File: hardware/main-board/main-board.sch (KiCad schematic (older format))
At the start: 12 parts

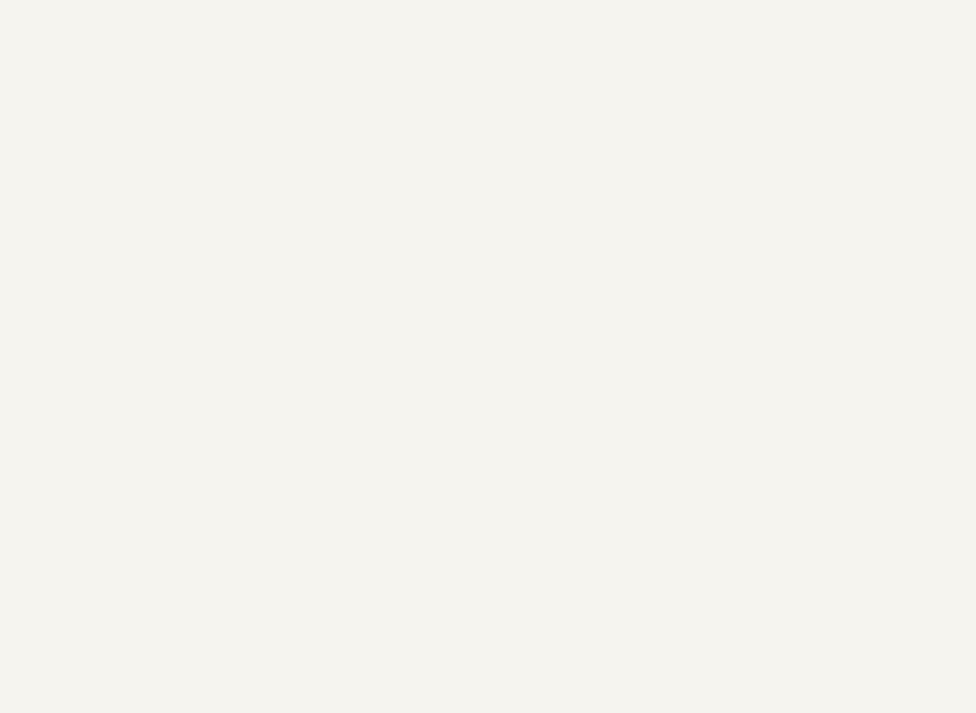
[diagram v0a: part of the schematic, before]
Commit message: Sound to light board completed, PSU board completed
Rev As as ordered
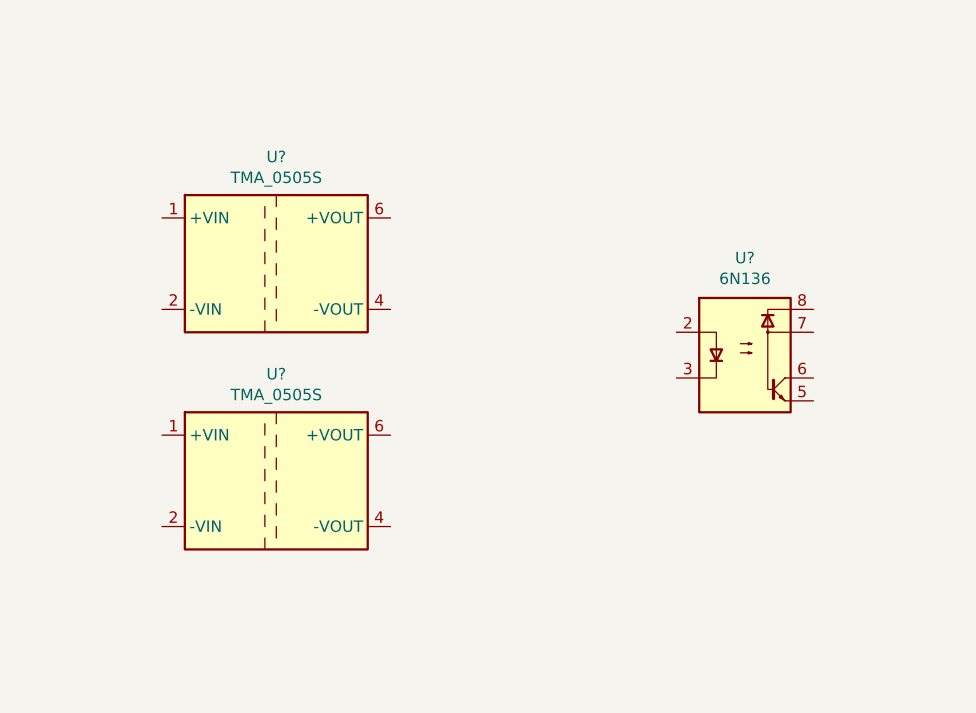
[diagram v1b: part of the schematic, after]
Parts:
- added U? (x2): TMA_0505S, Converter_DCDC:Traco_TMA_DCDCsingle, symbol Regulator_Switching:TMA_0505S
- added U?: 6N136, Package_DIP:DIP-8_W7.62mm, symbol Isolator:6N136
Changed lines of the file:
@@
 NoConn ~ 2600 6800
 NoConn ~ 2600 6900
+$Comp
+L Regulator_Switching:TMA_0505S U?
+U 1 1 5E9BA76B
+P 4000 1650
+F 0 "U?" H 4000 2117 50  0000 C CNN
+F 1 "TMA_0505S" H 4000 2026 50  0000 C CNN
+F 2 "Converter_DCDC:Traco_TMA_DCDCsingle" H 4000 1300 50  0001 C CNN
+F 3 "http://assets.tracopower.com/TMR1/documents/tmr1-datasheet.pdf" H 4000 1150 50  0001 C CNN
+	1    4000 1650
+	1    0    0    -1
+$EndComp
+$Comp
+L Regulator_Switching:TMA_0505S U?
+U 1 1 5E9BC0CB
+P 4000 2600
+F 0 "U?" H 4000 3067 50  0000 C CNN
+F 1 "TMA_0505S" H 4000 2976 50  0000 C CNN
+F 2 "Converter_DCDC:Traco_TMA_DCDCsingle" H 4000 2250 50  0001 C CNN
+F 3 "http://assets.tracopower.com/TMR1/documents/tmr1-datasheet.pdf" H 4000 2100 50  0001 C CNN
+	1    4000 2600
+	1    0    0    -1
+$EndComp
+$Comp
+L Isolator:6N136 U?
+U 1 1 5E9BE7CA
+P 6050 2050
+F 0 "U?" H 6050 2475 50  0000 C CNN
+F 1 "6N136" H 6050 2384 50  0000 C CNN
+F 2 "Package_DIP:DIP-8_W7.62mm" H 5850 1750 50  0001 L CIN
+F 3 "https://optoelectronics.liteon.com/upload/download/DS70-2008-0032/6N135-L%206N136-L%20series.pdf" H 6050 2050 50  0001 L CNN
+	1    6050 2050
+	1    0    0    -1
+$EndComp
 $EndSCHEMATC

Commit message: Motherboard Rev A
PCB as ordered
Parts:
- removed J? (x2): XLR5, symbol Connector:XLR5
- added C1, C2: 470nF, Capacitor_THT:C_Rect_L7.2mm_W5.5mm_P5.00mm_FKS2_FKP2_MKS2_MKP2, symbol Device:C
- added C3: 10uF, Capacitor_THT:CP_Radial_D6.3mm_P2.50mm, symbol Device:CP
- added J1: DMX_In_Connector, Connector_PinHeader_2.54mm:Krone_4_Way_terminal, symbol Connector:Conn_01x04_Female
- added J2: DMX_Out_Connector, Connector_PinHeader_2.54mm:Krone_4_Way_terminal, symbol Connector:Conn_01x04_Female
- added J7: SD_Card_Connector_1, Connector_PinHeader_2.54mm:Molex_KK254_1x04Vertical, symbol Connector:Conn_01x04_Male
- added J9: SD_Card_Connector_2, Connector_PinHeader_2.54mm:Molex_KK254_1x04Vertical, symbol Connector:Conn_01x04_Male
- added R1, R7: 470R, Resistor_THT:R_Axial_DIN0207_L6.3mm_D2.5mm_P10.16mm_Horizontal, symbol Device:R
- added R2, R5: 4.7k, Resistor_THT:R_Axial_DIN0207_L6.3mm_D2.5mm_P10.16mm_Horizontal, symbol Device:R
- added R3, R4, R6: 120R, Resistor_THT:R_Axial_DIN0207_L6.3mm_D2.5mm_P10.16mm_Horizontal, symbol Device:R
- added R8: 10k, Resistor_THT:R_Axial_DIN0207_L6.3mm_D2.5mm_P10.16mm_Horizontal, symbol Device:R
- added U6: 6N136, Package_DIP:DIP-8_W7.62mm_Socket, symbol Isolator:6N136
- J3, J4, J6: renamed from J?; footprint (none) -> Connector_PinHeader_2.54mm:Molex_KK254_1x04Vertical
- J5: renamed from J?; footprint (none) -> Connector_RJ:Krone_split_termials
- J8: renamed from J?; footprint (none) -> Connector_PinHeader_2.54mm:Molex_KK254_1x05Vertical
- U1: renamed from U?; value TMA_0505S -> DMX Input 5V Isolation
- U2: renamed from U?; footprint Package_DIP:DIP-8_W7.62mm -> Package_DIP:DIP-8_W7.62mm_Socket
- U3, U4: renamed from U?; footprint (none) -> Package_DIP:DIP-8_W7.62mm_Socket
- U5: renamed from U?; value TMA_0505S -> DMX Output 5V Isolation
- gave numbers to parts that had none: 3
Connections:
- net labels added: +3.3V, +5VL, BUTTON_1, BUTTON_2, BUTTON_4, CLK, CS_D3, LED_1, LED_2, LED_4, MISO_D0, MOSI_CMD
- wire segments 68 -> 157
- no-connect marks 15 -> 10
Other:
- moved on the sheet: J3, J4, J5, J6, J8, U1, U2, U5, U7

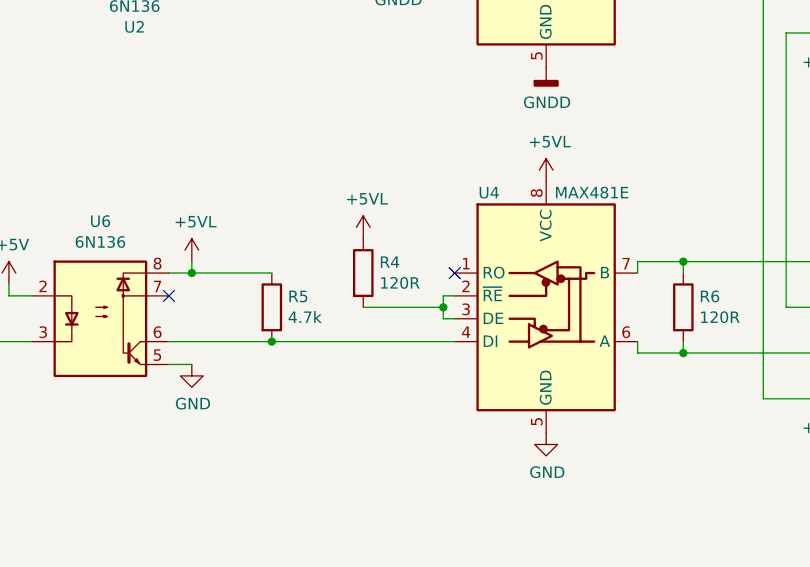
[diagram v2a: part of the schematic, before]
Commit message: PCB updates
Correction to motherboard R value, update of buttons PCB to rev B as ordered to go in case with reduced clearance
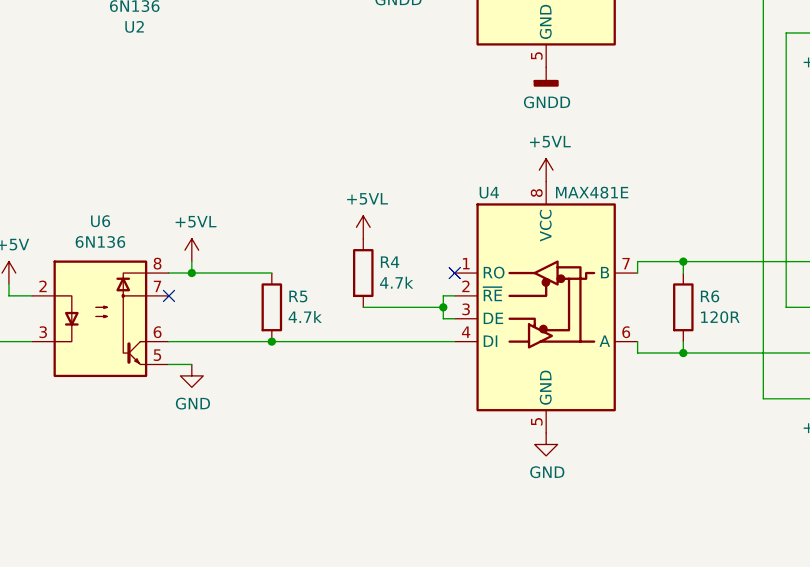
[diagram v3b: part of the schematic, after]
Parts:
- R4: value 120R -> 4.7k
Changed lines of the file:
@@
 P 7050 2800
 F 0 "R4" H 7120 2846 50  0000 L CNN
-F 1 "120R" H 7120 2755 50  0000 L CNN
+F 1 "4.7k" H 7120 2755 50  0000 L CNN
 F 2 "Resistor_THT:R_Axial_DIN0207_L6.3mm_D2.5mm_P10.16mm_Horizontal" V 6980 2800 50  0001 C CNN
 F 3 "~" H 7050 2800 50  0001 C CNN
